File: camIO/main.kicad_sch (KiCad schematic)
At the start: 28 parts, among them J1 MISC, J2 CSI/DSI, Q1 BSS138

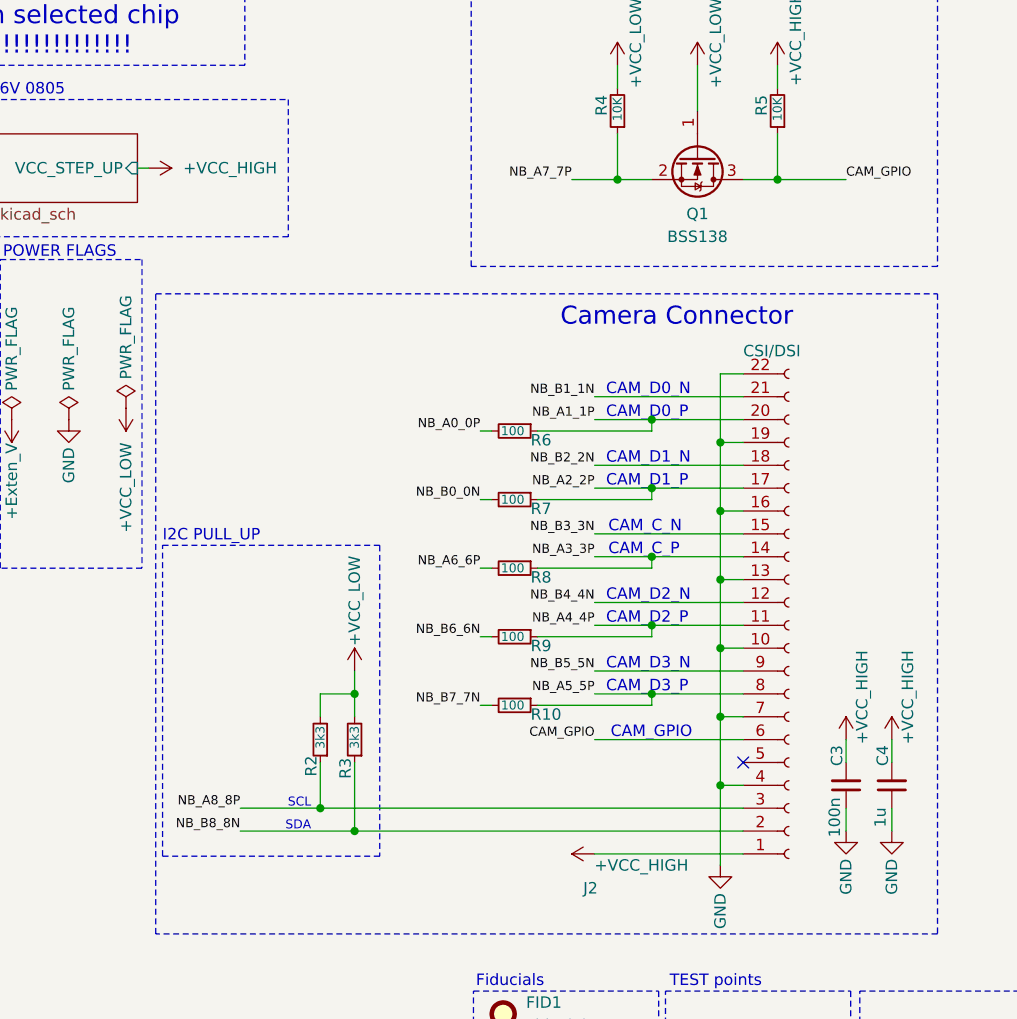
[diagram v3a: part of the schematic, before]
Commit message: Adding termination #4
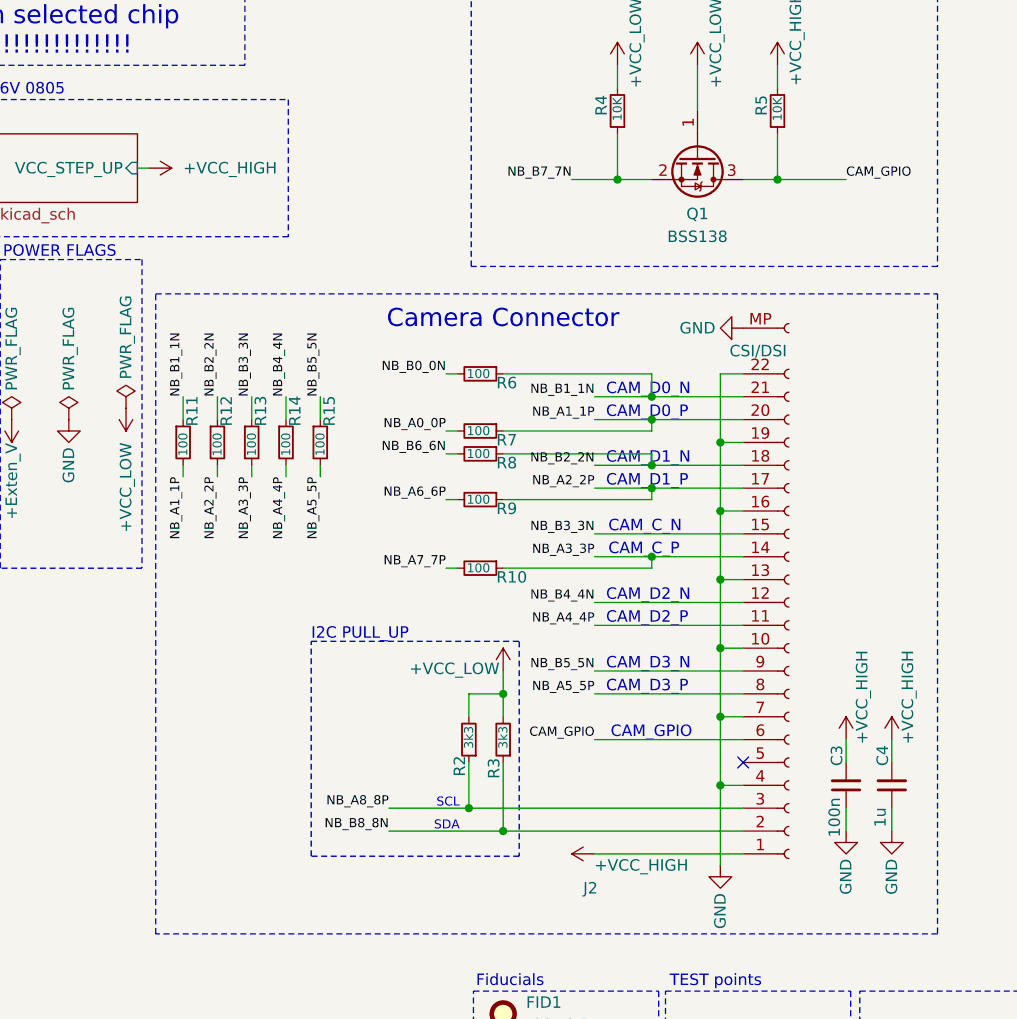
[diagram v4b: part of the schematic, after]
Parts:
- added R11, R12, R13, R14, R15: 100, Resistor_SMD:R_0402_1005Metric, symbol Device:R_Small
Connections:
- net GND: now also J2.MP
- net NB_A0_0P: now also R7.2; no longer R6.2
- net NB_A1_1P: now also R7.1, R11.2; no longer R6.1
- net NB_A2_2P: now also R9.1, R12.2; no longer R7.1
- net NB_A3_3P: now also R10.1, R13.2; no longer R8.1
- net NB_A4_4P: now also R14.2; no longer R9.1
- net NB_A5_5P: now also R15.2; no longer R10.1
- net NB_A6_6P: now also R9.2; no longer R8.2
- net NB_A7_7P: now also R10.2; no longer Q1.2 (S), R4.1
- net NB_B0_0N: now also R6.2; no longer R7.2
- net NB_B1_1N: now also R6.1, R11.1
- net NB_B2_2N: now also R8.1, R12.1
- net NB_B3_3N: now also R13.1
- net NB_B4_4N: now also R14.1
- net NB_B5_5N: now also R15.1
- net NB_B6_6N: now also R8.2; no longer R9.2
- net NB_B7_7N: now also Q1.2 (S), R4.1; no longer R10.2
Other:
- moved on the sheet: R10, R2, R3, R6, R7, R8, R9
